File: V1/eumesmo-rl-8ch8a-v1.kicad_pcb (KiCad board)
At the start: 2 copper layers, 98 x 67.8 mm, 48 parts, among them J1 250-202, J2 250-204, J3 250-204, J4 DB142V-5.08-4P, J5 DB142V-5.08-4P, J6 DB142V-5.08-4P, J7 DB142V-5.08-4P, K1 G5Q-1A4-DC24V, K2 G5Q-1A4-DC24V, K3 G5Q-1A4-DC24V, K4 G5Q-1A4-DC24V, K5 G5Q-1A4-DC24V, K6 G5Q-1A4-DC24V, K7 G5Q-1A4-DC24V, K8 G5Q-1A4-DC24V

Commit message: LEDs changed to orange
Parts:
- D1, D11, D13, D15, D3, D5, D7, D9: value EMERALD -> ORANGE/0603
- R1, R2, R3, R4, R5, R6, R7, R8: value 10k/125mW -> 9.1k/125mW
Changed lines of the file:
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@@
 			)
 		)
-		(property "Value" "EMERALD"
+		(property "Value" "ORANGE/0603"
 			(at 0 1.43 0)
 			(layer "F.Fab")
@@
 			)
 		)
-		(property "LCSC Part #" "C2984266"
+		(property "LCSC Part #" "C2987557"
 			(at 0 0 0)
 			(layer "F.Fab")
@@
 			)
 		)
-		(property "Mfr PN" "19-213/GHC-XS1T1N/5T"
+		(property "Mfr PN" "19-217/S2C-AL1M2VY/6T"
 			(at 0 0 0)
 			(layer "F.Fab")
@@
 			)
 		)
-		(property "Vendor PN" "C2984266"
+		(property "Vendor PN" "C2987557"
 			(at 0 0 0)
 			(layer "F.Fab")
@@
 			)
 		)
-		(property "Value" "10k/125mW"
+		(property "Value" "9.1k/125mW"
 			(at 0 1.65 180)
 			(layer "F.Fab")
@@
 			)
 		)
-		(property "Mfr PN" "0805W8F1002T5E"
+		(property "Mfr PN" "0805W8F9101T5E"
 			(at 0 0 180)
 			(unlocked yes)
@@
 			)
 		)
-		(property "Vendor PN" "C17414"
+		(property "Vendor PN" "C17855"
 			(at 0 0 180)
 			(unlocked yes)
@@
 			)
 		)
-		(property "LCSC Part #" "C17414"
+		(property "LCSC Part #" "C17855"
 			(at 0 0 180)
 			(unlocked yes)
@@
 			)
 		)
-		(property "Value" "10k/125mW"
+		(property "Value" "9.1k/125mW"
 			(at 0 1.65 180)
 			(layer "F.Fab")
@@
 			)
 		)
-		(property "Mfr PN" "0805W8F1002T5E"
+		(property "Mfr PN" "0805W8F9101T5E"
 			(at 0 0 180)
 			(unlocked yes)
@@
 			)
 		)
-		(property "Vendor PN" "C17414"
+		(property "Vendor PN" "C17855"
 			(at 0 0 180)
 			(unlocked yes)
@@
 			)
 		)
-		(property "LCSC Part #" "C17414"
+		(property "LCSC Part #" "C17855"
 			(at 0 0 180)
 			(unlocked yes)
@@
 			)
 		)
-		(property "Value" "EMERALD"
+		(property "Value" "ORANGE/0603"
 			(at 0 1.43 0)
 			(layer "F.Fab")
@@
 			)
 		)
-		(property "LCSC Part #" "C2984266"
+		(property "LCSC Part #" "C2987557"
 			(at 0 0 0)
 			(layer "F.Fab")
@@
 			)
 		)
-		(property "Mfr PN" "19-213/GHC-XS1T1N/5T"
+		(property "Mfr PN" "19-217/S2C-AL1M2VY/6T"
 			(at 0 0 0)
 			(layer "F.Fab")
@@
 			)
 		)
-		(property "Vendor PN" "C2984266"
+		(property "Vendor PN" "C2987557"
 			(at 0 0 0)
 			(layer "F.Fab")
@@
 			)
 		)
-		(property "Value" "10k/125mW"
+		(property "Value" "9.1k/125mW"
 			(at 0 1.65 180)
 			(layer "F.Fab")
@@
 			)
 		)
-		(property "Mfr PN" "0805W8F1002T5E"
+		(property "Mfr PN" "0805W8F9101T5E"
 			(at 0 0 180)
 			(unlocked yes)
@@
 			)
 		)
-		(property "Vendor PN" "C17414"
+		(property "Vendor PN" "C17855"
 			(at 0 0 180)
 			(unlocked yes)
@@
 			)
 		)
-		(property "LCSC Part #" "C17414"
+		(property "LCSC Part #" "C17855"
 			(at 0 0 180)
 			(unlocked yes)
@@
 			)
 		)
-		(property "Value" "EMERALD"
+		(property "Value" "ORANGE/0603"
 			(at 0 1.43 0)
 			(layer "F.Fab")
@@
 			)
 		)
-		(property "LCSC Part #" "C2984266"
+		(property "LCSC Part #" "C2987557"
 			(at 0 0 0)
 			(layer "F.Fab")
@@
 			)
 		)
-		(property "Mfr PN" "19-213/GHC-XS1T1N/5T"
+		(property "Mfr PN" "19-217/S2C-AL1M2VY/6T"
 			(at 0 0 0)
 			(layer "F.Fab")
@@
 			)
 		)
-		(property "Vendor PN" "C2984266"
+		(property "Vendor PN" "C2987557"
 			(at 0 0 0)
 			(layer "F.Fab")
@@
 			)
 		)
-		(property "Value" "EMERALD"
+		(property "Value" "ORANGE/0603"
 			(at 0 1.43 0)
 			(layer "F.Fab")
@@
 			)
 		)
-		(property "LCSC Part #" "C2984266"
+		(property "LCSC Part #" "C2987557"
 			(at 0 0 0)
 			(layer "F.Fab")
@@
 			)
 		)
-		(property "Mfr PN" "19-213/GHC-XS1T1N/5T"
+		(property "Mfr PN" "19-217/S2C-AL1M2VY/6T"
 			(at 0 0 0)
 			(layer "F.Fab")
@@
 			)
 		)
-		(property "Vendor PN" "C2984266"
+		(property "Vendor PN" "C2987557"
 			(at 0 0 0)
 			(layer "F.Fab")
@@
 			)
 		)
-		(property "Value" "10k/125mW"
+		(property "Value" "9.1k/125mW"
 			(at 0 1.65 180)
 			(layer "F.Fab")
@@
 			)
 		)
-		(property "Mfr PN" "0805W8F1002T5E"
+		(property "Mfr PN" "0805W8F9101T5E"
 			(at 0 0 180)
 			(unlocked yes)
@@
 			)
 		)
-		(property "Vendor PN" "C17414"
+		(property "Vendor PN" "C17855"
 			(at 0 0 180)
 			(unlocked yes)
@@
 			)
 		)
-		(property "LCSC Part #" "C17414"
+		(property "LCSC Part #" "C17855"
 			(at 0 0 180)
 			(unlocked yes)
@@
 			)
 		)
-		(property "Value" "10k/125mW"
+		(property "Value" "9.1k/125mW"
 			(at 0 1.65 180)
 			(layer "F.Fab")
@@
 			)
 		)
-		(property "Mfr PN" "0805W8F1002T5E"
+		(property "Mfr PN" "0805W8F9101T5E"
 			(at 0 0 180)
 			(unlocked yes)
@@
 			)
 		)
-		(property "Vendor PN" "C17414"
+		(property "Vendor PN" "C17855"
 			(at 0 0 180)
 			(unlocked yes)
@@
 			)
 		)
-		(property "LCSC Part #" "C17414"
+		(property "LCSC Part #" "C17855"
 			(at 0 0 180)
 			(unlocked yes)
@@
 			)
 		)
-		(property "Value" "EMERALD"
+		(property "Value" "ORANGE/0603"
 			(at 0 1.43 0)
 			(layer "F.Fab")
@@
 			)
 		)
-		(property "LCSC Part #" "C2984266"
+		(property "LCSC Part #" "C2987557"
 			(at 0 0 0)
 			(layer "F.Fab")
@@
 			)
 		)
-		(property "Mfr PN" "19-213/GHC-XS1T1N/5T"
+		(property "Mfr PN" "19-217/S2C-AL1M2VY/6T"
 			(at 0 0 0)
 			(layer "F.Fab")
@@
 			)
 		)
-		(property "Vendor PN" "C2984266"
+		(property "Vendor PN" "C2987557"
 			(at 0 0 0)
 			(layer "F.Fab")
@@
 			)
 		)
-		(property "Value" "10k/125mW"
+		(property "Value" "9.1k/125mW"
 			(at 0 1.65 180)
 			(layer "F.Fab")
@@
 			)
 		)
-		(property "Mfr PN" "0805W8F1002T5E"
+		(property "Mfr PN" "0805W8F9101T5E"
 			(at 0 0 180)
 			(unlocked yes)
@@
 			)
 		)
-		(property "Vendor PN" "C17414"
+		(property "Vendor PN" "C17855"
 			(at 0 0 180)
 			(unlocked yes)
@@
 			)
 		)
-		(property "LCSC Part #" "C17414"
+		(property "LCSC Part #" "C17855"
 			(at 0 0 180)
 			(unlocked yes)
@@
 			)
 		)
-		(property "Value" "EMERALD"
+		(property "Value" "ORANGE/0603"
 			(at 0 1.43 0)
 			(layer "F.Fab")
@@
 			)
 		)
-		(property "LCSC Part #" "C2984266"
+		(property "LCSC Part #" "C2987557"
 			(at 0 0 0)
 			(layer "F.Fab")
@@
 			)
 		)
-		(property "Mfr PN" "19-213/GHC-XS1T1N/5T"
+		(property "Mfr PN" "19-217/S2C-AL1M2VY/6T"
 			(at 0 0 0)
 			(layer "F.Fab")
@@
 			)
 		)
-		(property "Vendor PN" "C2984266"
+		(property "Vendor PN" "C2987557"
 			(at 0 0 0)
 			(layer "F.Fab")
@@
 			)
 		)
-		(property "Value" "10k/125mW"
+		(property "Value" "9.1k/125mW"
 			(at 0 1.65 180)
 			(layer "F.Fab")
@@
 			)
 		)
-		(property "Mfr PN" "0805W8F1002T5E"
+		(property "Mfr PN" "0805W8F9101T5E"
 			(at 0 0 180)
 			(unlocked yes)
@@
 			)
 		)
-		(property "Vendor PN" "C17414"
+		(property "Vendor PN" "C17855"
 			(at 0 0 180)
 			(unlocked yes)
@@
 			)
 		)
-		(property "LCSC Part #" "C17414"
+		(property "LCSC Part #" "C17855"
 			(at 0 0 180)
 			(unlocked yes)
@@
 			)
 		)
-		(property "Value" "EMERALD"
+		(property "Value" "ORANGE/0603"
 			(at 0 1.43 0)
 			(layer "F.Fab")
@@
 			)
 		)
-		(property "LCSC Part #" "C2984266"
+		(property "LCSC Part #" "C2987557"
 			(at 0 0 0)
 			(layer "F.Fab")
@@
 			)
 		)
-		(property "Mfr PN" "19-213/GHC-XS1T1N/5T"
+		(property "Mfr PN" "19-217/S2C-AL1M2VY/6T"
 			(at 0 0 0)
 			(layer "F.Fab")
@@
 			)
 		)
-		(property "Vendor PN" "C2984266"
+		(property "Vendor PN" "C2987557"
 			(at 0 0 0)
 			(layer "F.Fab")
@@
 			)
 		)
-		(property "Value" "10k/125mW"
+		(property "Value" "9.1k/125mW"
 			(at 0 1.65 180)
 			(layer "F.Fab")
@@
 			)
 		)
-		(property "Mfr PN" "0805W8F1002T5E"
+		(property "Mfr PN" "0805W8F9101T5E"
 			(at 0 0 180)
 			(unlocked yes)
@@
 			)
 		)
-		(property "Vendor PN" "C17414"
+		(property "Vendor PN" "C17855"
 			(at 0 0 180)
 			(unlocked yes)
@@
 			)
 		)
-		(property "LCSC Part #" "C17414"
+		(property "LCSC Part #" "C17855"
 			(at 0 0 180)
 			(unlocked yes)
@@
 			)
 		)
-		(property "Value" "EMERALD"
+		(property "Value" "ORANGE/0603"
 			(at 0 1.43 0)
 			(layer "F.Fab")
@@
 			)
 		)
-		(property "LCSC Part #" "C2984266"
+		(property "LCSC Part #" "C2987557"
 			(at 0 0 0)
 			(layer "F.Fab")
@@
 			)
 		)
-		(property "Mfr PN" "19-213/GHC-XS1T1N/5T"
+		(property "Mfr PN" "19-217/S2C-AL1M2VY/6T"
 			(at 0 0 0)
 			(layer "F.Fab")
@@
 			)
 		)
-		(property "Vendor PN" "C2984266"
+		(property "Vendor PN" "C2987557"
 			(at 0 0 0)
 			(layer "F.Fab")

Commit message: LEDs replaced for orange
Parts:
- R1, R2, R3, R4, R5, R6, R7, R8: value 9.1k/125mW -> 10k/125mW
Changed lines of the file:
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@@
 			)
 		)
-		(property "Value" "9.1k/125mW"
+		(property "Value" "10k/125mW"
 			(at 0 1.65 180)
 			(layer "F.Fab")
@@
 			)
 		)
-		(property "Mfr PN" "0805W8F9101T5E"
+		(property "Mfr PN" "0805W8F1002T5E"
 			(at 0 0 180)
 			(unlocked yes)
@@
 			)
 		)
-		(property "Vendor PN" "C17855"
+		(property "Vendor PN" "C17414"
 			(at 0 0 180)
 			(unlocked yes)
@@
 			)
 		)
-		(property "LCSC Part #" "C17855"
+		(property "LCSC Part #" "C17414"
 			(at 0 0 180)
 			(unlocked yes)
@@
 			)
 		)
-		(property "Value" "9.1k/125mW"
+		(property "Value" "10k/125mW"
 			(at 0 1.65 180)
 			(layer "F.Fab")
@@
 			)
 		)
-		(property "Mfr PN" "0805W8F9101T5E"
+		(property "Mfr PN" "0805W8F1002T5E"
 			(at 0 0 180)
 			(unlocked yes)
@@
 			)
 		)
-		(property "Vendor PN" "C17855"
+		(property "Vendor PN" "C17414"
 			(at 0 0 180)
 			(unlocked yes)
@@
 			)
 		)
-		(property "LCSC Part #" "C17855"
+		(property "LCSC Part #" "C17414"
 			(at 0 0 180)
 			(unlocked yes)
@@
 			)
 		)
-		(property "Value" "9.1k/125mW"
+		(property "Value" "10k/125mW"
 			(at 0 1.65 180)
 			(layer "F.Fab")
@@
 			)
 		)
-		(property "Mfr PN" "0805W8F9101T5E"
+		(property "Mfr PN" "0805W8F1002T5E"
 			(at 0 0 180)
 			(unlocked yes)
@@
 			)
 		)
-		(property "Vendor PN" "C17855"
+		(property "Vendor PN" "C17414"
 			(at 0 0 180)
 			(unlocked yes)
@@
 			)
 		)
-		(property "LCSC Part #" "C17855"
+		(property "LCSC Part #" "C17414"
 			(at 0 0 180)
 			(unlocked yes)
@@
 			)
 		)
-		(property "Value" "9.1k/125mW"
+		(property "Value" "10k/125mW"
 			(at 0 1.65 180)
 			(layer "F.Fab")
@@
 			)
 		)
-		(property "Mfr PN" "0805W8F9101T5E"
+		(property "Mfr PN" "0805W8F1002T5E"
 			(at 0 0 180)
 			(unlocked yes)
@@
 			)
 		)
-		(property "Vendor PN" "C17855"
+		(property "Vendor PN" "C17414"
 			(at 0 0 180)
 			(unlocked yes)
@@
 			)
 		)
-		(property "LCSC Part #" "C17855"
+		(property "LCSC Part #" "C17414"
 			(at 0 0 180)
 			(unlocked yes)
@@
 			)
 		)
-		(property "Value" "9.1k/125mW"
+		(property "Value" "10k/125mW"
 			(at 0 1.65 180)
 			(layer "F.Fab")
@@
 			)
 		)
-		(property "Mfr PN" "0805W8F9101T5E"
+		(property "Mfr PN" "0805W8F1002T5E"
 			(at 0 0 180)
 			(unlocked yes)
@@
 			)
 		)
-		(property "Vendor PN" "C17855"
+		(property "Vendor PN" "C17414"
 			(at 0 0 180)
 			(unlocked yes)
@@
 			)
 		)
-		(property "LCSC Part #" "C17855"
+		(property "LCSC Part #" "C17414"
 			(at 0 0 180)
 			(unlocked yes)
@@
 			)
 		)
-		(property "Value" "9.1k/125mW"
+		(property "Value" "10k/125mW"
 			(at 0 1.65 180)
 			(layer "F.Fab")
@@
 			)
 		)
-		(property "Mfr PN" "0805W8F9101T5E"
+		(property "Mfr PN" "0805W8F1002T5E"
 			(at 0 0 180)
 			(unlocked yes)
@@
 			)
 		)
-		(property "Vendor PN" "C17855"
+		(property "Vendor PN" "C17414"
 			(at 0 0 180)
 			(unlocked yes)
@@
 			)
 		)
-		(property "LCSC Part #" "C17855"
+		(property "LCSC Part #" "C17414"
 			(at 0 0 180)
 			(unlocked yes)
@@
 			)
 		)
-		(property "Value" "9.1k/125mW"
+		(property "Value" "10k/125mW"
 			(at 0 1.65 180)
 			(layer "F.Fab")
@@
 			)
 		)
-		(property "Mfr PN" "0805W8F9101T5E"
+		(property "Mfr PN" "0805W8F1002T5E"
 			(at 0 0 180)
 			(unlocked yes)
@@
 			)
 		)
-		(property "Vendor PN" "C17855"
+		(property "Vendor PN" "C17414"
 			(at 0 0 180)
 			(unlocked yes)
@@
 			)
 		)
-		(property "LCSC Part #" "C17855"
+		(property "LCSC Part #" "C17414"
 			(at 0 0 180)
 			(unlocked yes)
@@
 			)
 		)
-		(property "Value" "9.1k/125mW"
+		(property "Value" "10k/125mW"
 			(at 0 1.65 180)
 			(layer "F.Fab")
@@
 			)
 		)
-		(property "Mfr PN" "0805W8F9101T5E"
+		(property "Mfr PN" "0805W8F1002T5E"
 			(at 0 0 180)
 			(unlocked yes)
@@
 			)
 		)
-		(property "Vendor PN" "C17855"
+		(property "Vendor PN" "C17414"
 			(at 0 0 180)
 			(unlocked yes)
@@
 			)
 		)
-		(property "LCSC Part #" "C17855"
+		(property "LCSC Part #" "C17414"
 			(at 0 0 180)
 			(unlocked yes)

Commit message: Adjusted comment regarding DIN rail modules.
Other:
- board text added: "SUPORTES PCI METALTEX SP7 MÓDULO EUMESMO-RL-8CH8A-V1 1x pé macho 9 mm 1x pé fêmea 9 mm 1x espaçador 45 mm 1x espaçador 20 mm 1x espaçador 15 mm Comprimento total 98 mm Largura da placa 67,8 mm"
- board text removed: "SUPORTES PCI METALTEX SP7 1x pé macho 9 mm 1x pé fêmea 9 mm 1x espaçador 45 mm 1x espaçador 20 mm 1x espaçador 15 mm Comprimento total 98 mm Largura da placa 67,8 mm"
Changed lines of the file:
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@@
 		)
 	)
-	(gr_text "SUPORTES PCI METALTEX SP7\n1x pé macho  9 mm\n1x pé fêmea 9 mm\n1x espaçador 45 mm\n1x espaçador 20 mm\n1x espaçador 15 mm\nComprimento total 98 mm\nLargura da placa 67,8 mm"
+	(gr_text "SUPORTES PCI METALTEX SP7\nMÓDULO EUMESMO-RL-8CH8A-V1\n1x pé macho  9 mm\n1x pé fêmea 9 mm\n1x espaçador 45 mm\n1x espaçador 20 mm\n1x espaçador 15 mm\nComprimento total 98 mm\nLargura da placa 67,8 mm"
 		(at 125 132 0)
 		(layer "Cmts.User")

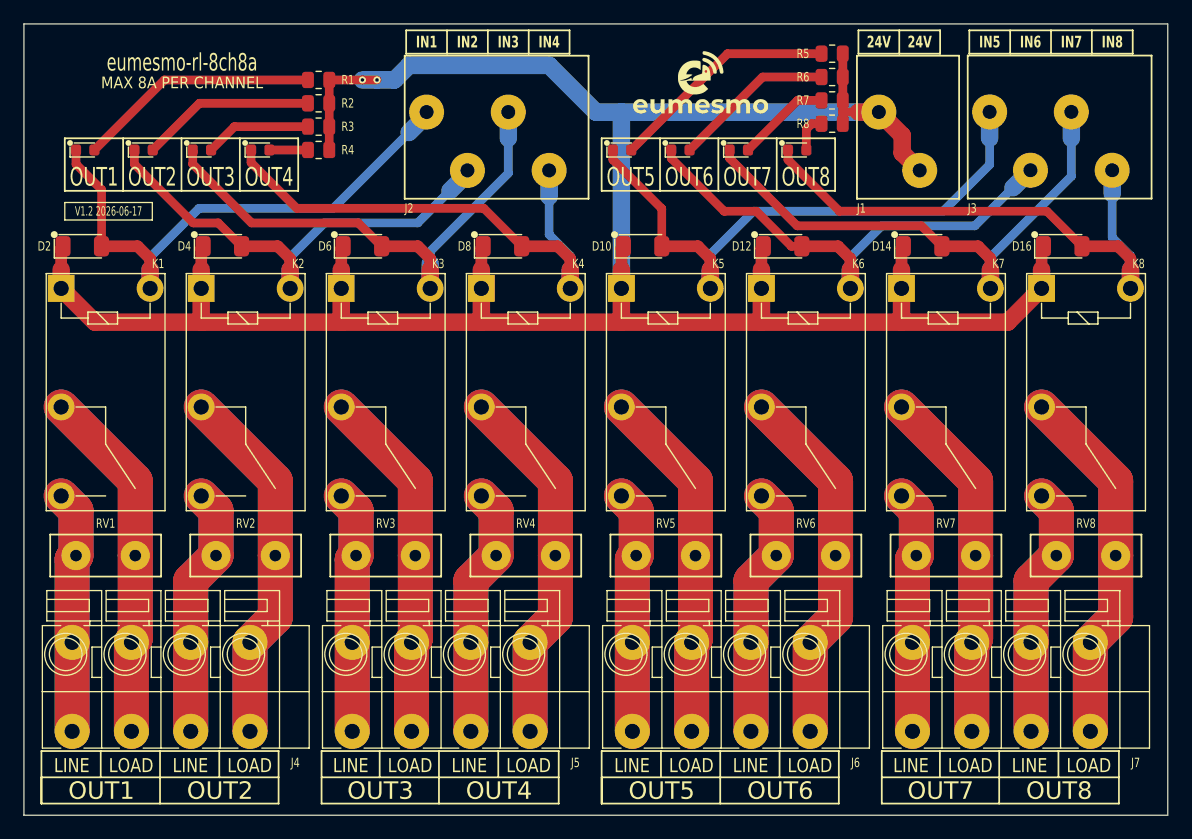
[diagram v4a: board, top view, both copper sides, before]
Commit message: Adjusted terminal block positions
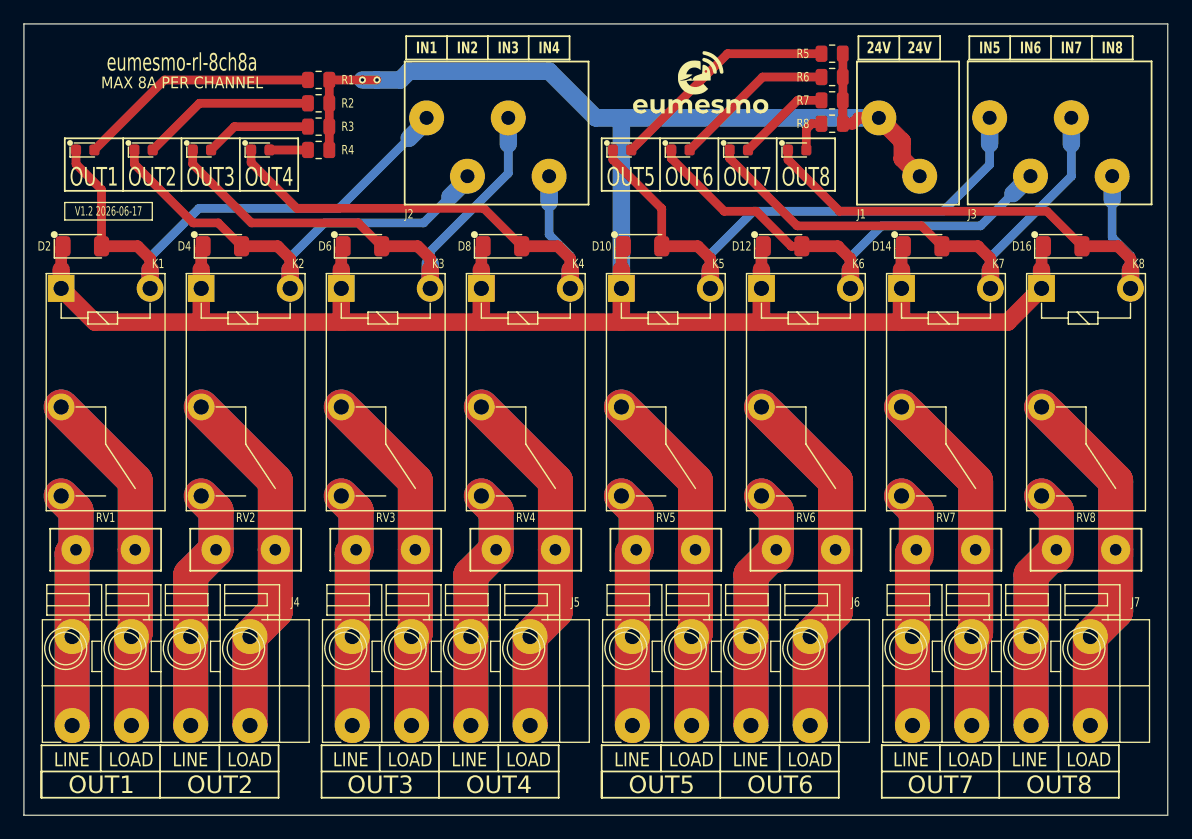
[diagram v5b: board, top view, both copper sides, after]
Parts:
- moved J1 0.50 mm to (200.0, 72.8)
- moved J2 0.50 mm to (164.8, 72.8)
- moved J3 0.50 mm to (213.0, 72.7)
- moved J4 0.50 mm to (136.8, 118.5)
- moved J5 0.50 mm to (160.8, 118.5)
- moved J6 0.50 mm to (184.8, 118.5)
- moved J7 0.50 mm to (208.8, 118.5)
- moved RV1 0.50 mm to (132.0, 107.2)
- moved RV2 0.50 mm to (144.0, 107.2)
- moved RV3 0.50 mm to (156.0, 107.2)
- moved RV4 0.50 mm to (168.0, 107.2)
- moved RV5 0.50 mm to (180.0, 107.2)
- moved RV6 0.50 mm to (192.0, 107.2)
- moved RV7 0.50 mm to (204.0, 107.2)
- moved RV8 0.50 mm to (216.0, 107.2)
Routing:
- net /OUT5LN: track 41.7 -> 40.7 mm
- net /OUT4LN: track 43.2 -> 42.2 mm
- net /OUT4LD: track 62.6 -> 61.6 mm
- net /OUT3LN: track 41.7 -> 40.7 mm
- net /OUT3LD: track 61.1 -> 60.1 mm
- net /OUT2LN: track 43.2 -> 42.2 mm
- net /OUT2LD: track 62.6 -> 61.6 mm
- net /OUT1LN: track 41.7 -> 40.7 mm
- net /OUT5LD: track 61.1 -> 60.1 mm
- net /OUT1LD: track 61.1 -> 60.1 mm
- net /OUT8LN: track 43.2 -> 42.7 mm
- net /OUT8LD: track 62.6 -> 62.1 mm
- net /OUT7LN: track 41.7 -> 41.2 mm
- net /OUT6LN: track 43.2 -> 42.7 mm
- net /OUT6LD: track 62.6 -> 62.1 mm
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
